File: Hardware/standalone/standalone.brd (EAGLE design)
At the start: 100 x 80 mm, 92 parts, among them IC1 STM32F050C6T6A, IC2 AP1212, Q2 32.768khz, U1 DMS3016SSS-13, U2 DMS3016SSS-13, U3 DMS3016SSS-13, U4 LM2576S, U5 NMOS_2N7002, U6 NMOS_2N7002, X1 KUSBVX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

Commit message: Major PCB Re-arrangements and Fixes
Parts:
- RSENSE2, RSENSE_BATT: value 0.005 -> 0.1
- moved SERIAL 69.0 mm to (32.0, 56.0), turned to 90 degrees
- moved BUZZ1 54.9 mm to (91.0, 47.0), turned to 180 degrees
- moved D6 40.6 mm to (79.0, 41.0), turned to 90 degrees
- moved L_5V 38.5 mm to (90.0, 32.0), turned to 90 degrees
- moved 5V_CIN 27.8 mm to (61.0, 14.0), turned to 0 degrees
- moved R4 23.6 mm to (36.0, 64.0), turned to 270 degrees
- moved 5V_COUT 23.2 mm to (76.9, 13.8), turned to 0 degrees
- moved SOL 22.2 mm to (11.9, 74.7)
- moved C19 22.0 mm to (22.0, 77.0), turned to 90 degrees
- moved R_GAIN 22.0 mm to (25.0, 77.0), turned to 90 degrees
- moved SENSE_AMP_SOL 21.9 mm to (19.0, 77.0)
- moved C7 21.6 mm to (39.0, 64.0), turned to 270 degrees
- moved C6 20.1 mm to (53.0, 65.0)
- moved R3 18.9 mm to (33.0, 64.0)
- moved IC2 18.1 mm to (72.0, 37.0), turned to 180 degrees
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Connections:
- net CC_~EN renamed CC_EN
- removed net N$9: C10.1, C11.2, C4.+, D2.A, GATE_DRIVE.1, R1.2, RSENSE2.2, SENSE_AMP_SOL.2, U1.1, U1.2, U1.3
- new net N$38: RSENSE2.1, SENSE_AMP_SOL.3, SOL.3
- net N$16: now also C10.1, C11.2, C4.+, D2.A, GATE_DRIVE.1, R1.2, RSENSE2.2, SENSE_AMP_SOL.2, U1.1, U1.2, U1.3; no longer RSENSE2.1, SENSE_AMP_SOL.3, SOL.3
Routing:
- net N$9: track 152.1 -> 0.00 mm, vias 6 -> 4
- net +5V: track 157.4 -> 27.7 mm, vias 6 -> 0
- net N$16: track 21.2 -> 139.4 mm, vias 0 -> 3
- net N$22: track 8.32 -> 59.8 mm, vias 0 -> 1
- net USB_OUT1: track 47.5 -> 24.3 mm
- net USB_OUT2: track 57.1 -> 33.9 mm
- net N$12: track 27.7 -> 7.52 mm
- net SOL_I: track 51.1 -> 67.6 mm
- net USB_FLG2: track 49.1 -> 33.0 mm
- net USB_EN2: track 60.3 -> 45.2 mm
- net N$21: track 45.2 -> 31.1 mm
- net USB_FLG1: track 47.0 -> 33.5 mm
- net USART1_TX: track 0.00 -> 12.7 mm
- net USART1_RX: track 0.00 -> 10.7 mm
- net USB_EN1: track 61.6 -> 52.6 mm
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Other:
- board text removed: "Move Buzzer Swap Solar and Batt Connector"

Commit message: PCB 100% Routed
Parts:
- C20: value 10uF -> 1uF
- C8: value 1uF -> 10uF
- moved C5 20.0 mm to (58.0, 78.0)
- moved R2 20.0 mm to (54.0, 78.0)
- moved D3 5.00 mm to (40.0, 67.0), turned to 0 degrees
- moved C16 4.47 mm to (17.0, 24.0), turned to 90 degrees
- moved C10 2.83 mm to (32.0, 62.0)
- moved C7 2.83 mm to (41.0, 62.0)
- moved R3 2.83 mm to (35.0, 62.0)
- moved R4 2.83 mm to (38.0, 62.0)
- moved C4 2.24 mm to (32.0, 73.0)
- moved SERIAL 2.00 mm to (34.0, 56.0), turned to 0 degrees
- moved D6 1.00 mm to (80.0, 41.0), turned to 270 degrees
- moved L_MPPT 1.00 mm to (55.0, 74.0)
- moved U5 1.00 mm to (26.0, 9.00)
- moved U4 0.56 mm to (94.2, 9.50)
- turned C3 to 180 degrees
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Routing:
- net +5V: track 27.7 -> 150.3 mm, vias 0 -> 4
- net V_LOAD: track 227.4 -> 254.6 mm
- net N$12: track 7.52 -> 32.7 mm
- net GND: track 51.9 -> 72.4 mm, vias 8 -> 55
- net N$6: track 78.5 -> 59.0 mm
- net N$21: track 31.1 -> 41.2 mm
- net +3V3: track 175.6 -> 169.1 mm
- net BATT_I: track 54.3 -> 47.8 mm
- net N$16: track 139.4 -> 144.9 mm, vias 3 -> 8
- net SOL_V: track 50.8 -> 55.7 mm
- net CC_EN: track 74.0 -> 77.4 mm
- net USB_EN1: track 52.6 -> 55.8 mm
- net USART1_TX: track 12.7 -> 10.1 mm
- net USB_EN2: track 45.2 -> 47.4 mm
- net N$9: track 0.00 -> 2.00 mm
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
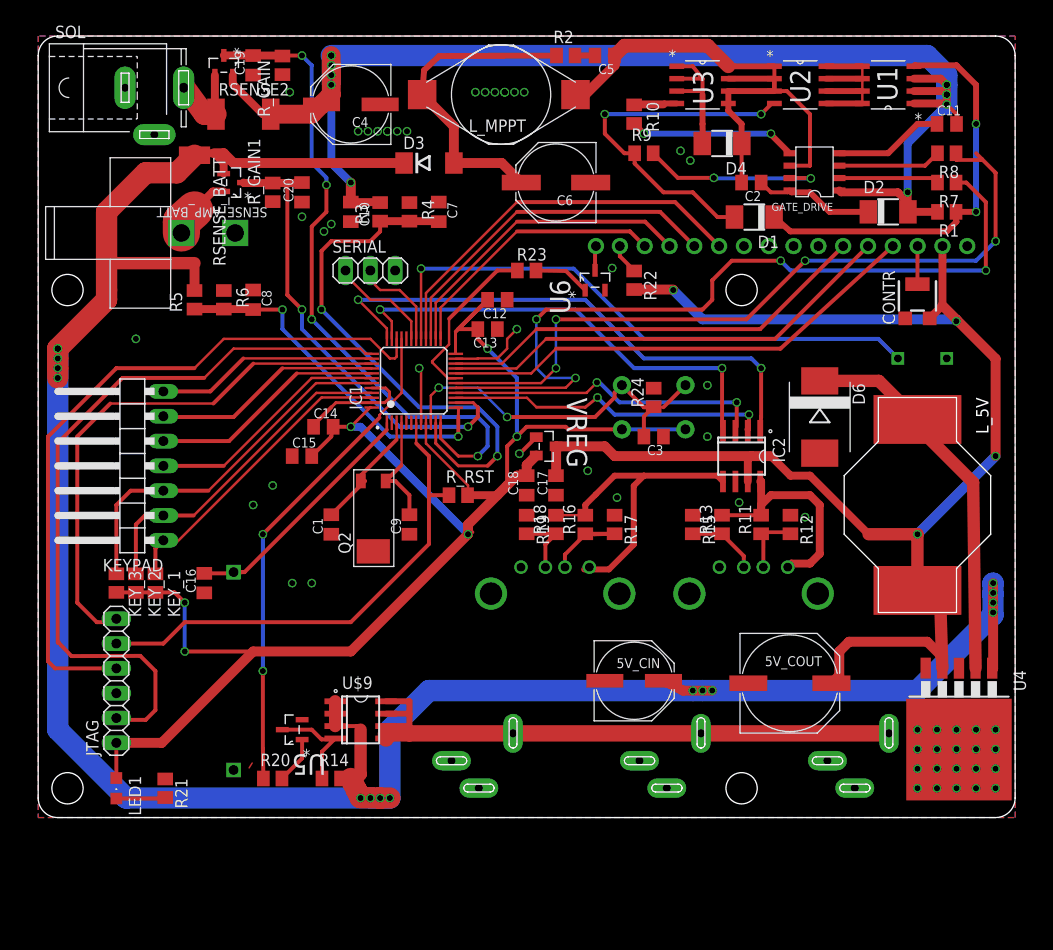
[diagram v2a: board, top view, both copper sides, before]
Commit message: PCB Fixes
LCD Power Switch Added.
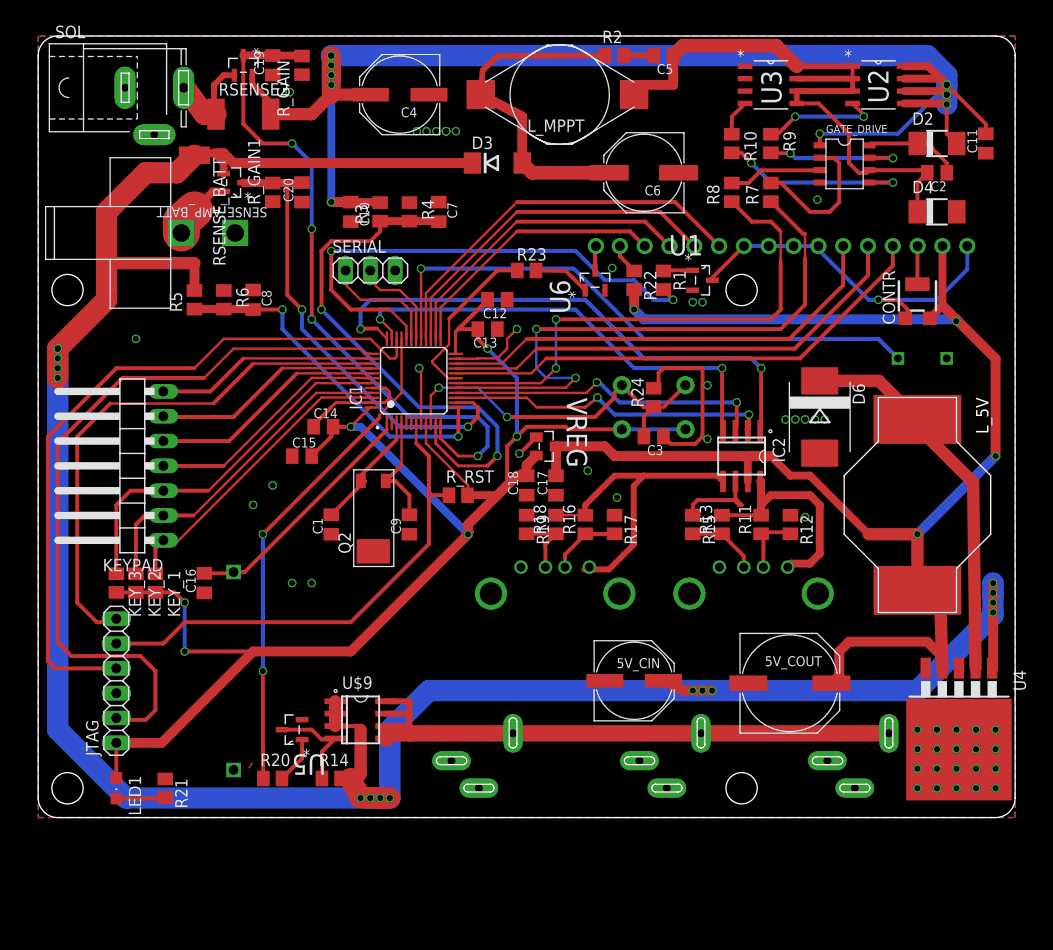
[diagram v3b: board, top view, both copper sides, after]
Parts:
- removed D1: S1A-E3/5AT, diode:DO-214AC
- R1: value 470K -> 1k; device rcl:M0805 -> resistor:M0805
- U1: value DMS3016SSS-13 -> NMOS_2N7002; device equinox:SOIC127P600X175-8N -> equinox:SOT103P240X110-3N
- moved R1 29.8 mm to (64.0, 55.0), turned to 270 degrees
- moved U1 27.6 mm to (68.0, 55.0), turned to 0 degrees
- moved D4 23.1 mm to (92.0, 62.0), turned to 0 degrees
- moved R8 22.4 mm to (71.0, 64.0), turned to 90 degrees
- moved C2 19.0 mm to (92.0, 66.0)
- moved R7 18.0 mm to (75.0, 64.0), turned to 90 degrees
- moved R9 13.0 mm to (75.0, 69.0), turned to 270 degrees
- moved R10 10.4 mm to (71.0, 69.0)
- moved C6 9.06 mm to (62.0, 66.0)
- moved D2 8.60 mm to (92.0, 69.0)
- moved U2 8.00 mm to (86.0, 75.0)
- moved D3 7.00 mm to (47.0, 67.0)
- moved U3 7.00 mm to (75.0, 75.0)
- moved C5 6.00 mm to (64.0, 78.0)
- moved L_MPPT 6.00 mm to (61.0, 74.0)
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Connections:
- new net LCD_PWR: IC1.32, R1.2
- net GND: now also U1.2; no longer CONTR.1, DIS1.1, DIS1.10, DIS1.7, DIS1.8, DIS1.9
- net N$14: no longer D1.A
- net N$16: now also U2.5, U2.6, U2.7, U2.8; no longer R1.2, U1.1, U1.2, U1.3
- net N$17: now also R1.1, U1.1; no longer U1.5, U1.6, U1.7, U1.8, U2.5, U2.6, U2.7, U2.8
- net N$5: now also CONTR.1, DIS1.1, DIS1.10, DIS1.7, DIS1.8, DIS1.9, U1.3; no longer D1.C, R1.1, U1.4
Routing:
- net LCD_PWR: track 0.00 -> 53.0 mm, vias 0 -> 2
- net N$14: track 37.2 -> 12.1 mm
- net CC_EN: track 77.4 -> 53.6 mm, vias 4 -> 2
- net CC_PWM: track 83.1 -> 61.8 mm, vias 4 -> 2
- net N$17: track 18.7 -> 3.01 mm
- net N$16: track 144.9 -> 155.5 mm
- net SOL_I: track 68.8 -> 76.2 mm
- net N$6: track 59.0 -> 66.3 mm
- net V_LOAD: track 254.6 -> 261.6 mm
- net N$5: track 42.9 -> 38.3 mm, vias 2 -> 1
- net N$8: track 10.2 -> 14.9 mm
- net N$7: track 19.4 -> 15.2 mm
- net N$13: track 17.2 -> 20.2 mm
- net LCD_E: track 44.6 -> 47.0 mm
- net N$12: track 32.7 -> 34.5 mm
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
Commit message: PCB Rev2  Complete. Ready for manufacture
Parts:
- removed RSENSE2, RSENSE_BATT: 0.1, rcl:R2512
- removed R_GAIN1: 1k65, rcl:M0805
- removed SENSE_AMP_BATT: ZXCT1107SA-7, equinox:SOT91P240X110-3N
- added R25, R26: 10K, rcl:M0805
- added R27, R28: 10, rcl:M0805
- added RS_B: 0.01, rcl:R2512
- added RS_S: 0.1, rcl:R2512
- added U7: INA213AIDCKT, equinox:SOT65P210X110-6N
- C20: value 1uF -> 10uF
- moved U$1 46.4 mm to (61.7, 35.9)
- moved C16 5.83 mm to (20.0, 29.0), turned to 270 degrees
- moved C20 5.39 mm to (22.0, 66.0)
- moved C10 5.00 mm to (32.0, 67.0)
- moved C7 5.00 mm to (41.0, 67.0)
- moved R3 5.00 mm to (35.0, 67.0)
- moved R4 5.00 mm to (38.0, 67.0)
- moved JTAG 4.47 mm to (6.00, 18.0)
- moved LED1 4.47 mm to (10.0, 7.00)
- moved KEY_1 4.12 mm to (16.0, 25.0)
- moved R21 4.00 mm to (13.0, 7.00)
- moved KEY_2 3.16 mm to (13.0, 25.0)
- moved KEY_3 2.24 mm to (10.0, 25.0)
- moved R1 2.00 mm to (62.0, 55.0)
- moved R2 2.00 mm to (61.0, 78.0)
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- renumbered R_GAIN to R30, SENSE_AMP_SOL to U10, U$9 to U9
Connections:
- new net N$39: R25.1, R26.2, U7.1
- new net N$40: C20.2, R27.1, U7.4
- new net N$41: C20.1, R28.1, U7.5
- net +3V3: now also R25.2, U7.3
- net BATT_I: now also U7.6; no longer C20.2, R_GAIN1.2, SENSE_AMP_BATT.1
- net GND: now also R26.1, U7.2; no longer C20.1, R_GAIN1.1
- net N$16: now also RS_S.2; no longer RSENSE2.2
- net N$38: now also RS_S.1; no longer RSENSE2.1
- net N$4: now also R28.2, RS_B.2; no longer RSENSE_BATT.2, SENSE_AMP_BATT.2
- net V_LOAD: now also R27.2, RS_B.1; no longer RSENSE_BATT.1, SENSE_AMP_BATT.3
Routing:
- net +3V3: track 169.1 -> 205.7 mm, vias 6 -> 7
- net V_LOAD: track 261.6 -> 291.3 mm
- net N$41: track 0.00 -> 10.6 mm
- net N$16: track 155.5 -> 148.2 mm, vias 8 -> 6
- net SWO: track 56.5 -> 49.5 mm
- net SWDIO: track 72.9 -> 66.4 mm
- net SOL_V: track 55.7 -> 61.8 mm
- net N$40: track 0.00 -> 5.30 mm
- net N$39: track 0.00 -> 5.19 mm
- net SWCLK: track 76.5 -> 72.6 mm
- net GND: track 73.7 -> 76.7 mm
- net BATT_I: track 47.8 -> 45.2 mm
- net N$37: track 5.04 -> 3.04 mm
- net N$12: track 34.5 -> 36.5 mm
- net N$32: track 5.85 -> 3.85 mm
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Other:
- board text added: "Design by Ashley Grealish - 2013"
- board text added: "M3 Bolt"
